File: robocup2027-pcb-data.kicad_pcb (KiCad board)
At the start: 6 copper layers, 83 x 117 mm, 47 parts, among them M5 Motor_Servo, M6 Motor_Servo, Q1 BPW40, Q2 BPW40, U1 ESP32-DEVKITC-32E

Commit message: updating pcb and step file
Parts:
- moved U12 31.5 mm to (151.9, 113.7)
- moved U4 27.9 mm to (120.6, 110.3)
- moved M6 12.8 mm to (128.3, 95.4)
- moved M5 10.3 mm to (149.7, 95.4)
- moved S1 0.78 mm to (121.4, 132.8)
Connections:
- U1 pad J2_12: unconnected-(U1-IO14-PadJ2_12) -> XSHUT1
- U1 pad J3_10: unconnected-(U1-IO5-PadJ3_10) -> XSHUT5
- U1 pad J3_16: unconnected-(U1-IO15-PadJ3_16) -> XSHUT6
- U1 pad J3_2: unconnected-(U1-IO23-PadJ3_2) -> XSHUT4
- U1 pad J3_8: unconnected-(U1-IO19-PadJ3_8) -> XSHUT3
- U1 pad J3_9: unconnected-(U1-IO18-PadJ3_9) -> XSHUT2
- U10 pad 5: unconnected-(U10-XSHUT-Pad5) -> XSHUT5
- U15 pad 5: unconnected-(U15-XSHUT-Pad5) -> XSHUT6
- U6 pad 5: unconnected-(U6-XSHUT-Pad5) -> XSHUT1
- U7 pad 5: unconnected-(U7-XSHUT-Pad5) -> XSHUT2
- U8 pad 5: unconnected-(U8-XSHUT-Pad5) -> XSHUT3
- U9 pad 5: unconnected-(U9-XSHUT-Pad5) -> XSHUT4

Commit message: some changes
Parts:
- moved U11 1.05 mm to (156.0, 56.8)
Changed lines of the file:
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@@
-		(embedded_fonts no)
-	)
-	(footprint "robo:DCDC-LTC3111"
-		(layer "F.Cu")
-		(at 155 56.5)
-		(property "Reference" "U11"
-			(at 0 -0.5 0)
-			(unlocked yes)
-			(layer "F.SilkS")
-			(effects
-				(font
-					(size 1 1)
-					(thickness 0.1)
-				)
-			)
-		)
-		(property "Value" "~"
-			(at 0 1 0)
-			(unlocked yes)
-			(layer "F.Fab")
-			(effects
-				(font
-					(size 1 1)
-					(thickness 0.15)
-				)
-			)
-		)
-		(property "Datasheet" ""
-			(at 0 0 0)
-			(unlocked yes)
-			(layer "F.Fab")
-			(hide yes)
-			(effects
-				(font
-					(size 1 1)
-					(thickness 0.15)
-				)
-			)
-		)
-		(property "Description" ""
-			(at 0 0 0)
-			(unlocked yes)
-			(layer "F.Fab")
-			(hide yes)
-			(effects
-				(font
-					(size 1 1)
-					(thickness 0.15)
-				)
-			)
-		)
-		(sheetname "/")
-		(sheetfile "robocup2027-pcb-data.kicad_sch")
-		(attr through_hole)
-		(fp_rect
-			(start -15 -15)
-			(end -15 15)
-			(stroke
-				(width 0.1)
-				(type default)
-			)
-			(fill no)
-			(layer "F.SilkS")
-		)
-		(fp_rect
-			(start -15 -15)
-			(end 15 -15)
-			(stroke
-				(width 0.1)
-				(type default)
-			)
-			(fill no)
-			(layer "F.SilkS")
-		)
-		(fp_rect
-			(start -15 15)
-			(end 15 15)
-			(stroke
-				(width 0.1)
-				(type default)
-			)
-			(fill no)
-			(layer "F.SilkS")
-		)
-		(fp_rect
-			(start 15 -15)
-			(end 15 15)
-			(stroke
-				(width 0.1)
-				(type default)
-			)
-			(fill no)
-			(layer "F.SilkS")
-		)
-		(fp_text user "Vout"
-			(at 6.1 -1.1 0)
-			(unlocked yes)
-			(layer "F.SilkS")
-			(effects
-				(font
-					(size 1 1)
-					(thickness 0.1)
-				)
-				(justify left bottom)
-			)
-		)
-		(fp_text user "Vin"
-			(at -9.2 -1.1 0)
-			(unlocked yes)
-			(layer "F.SilkS")
-			(effects
-				(font
-					(size 1 1)
-					(thickness 0.1)
-				)
-				(justify left bottom)
-			)
-		)
-		(fp_text user "GND"
-			(at 6.3 4.5 0)
-			(unlocked yes)
-			(layer "F.SilkS")
-			(effects
-				(font
-					(size 1 1)
-					(thickness 0.1)
-				)
-				(justify left bottom)
-			)
-		)
-		(fp_text user "GND"
-			(at -9.1 4.6 0)
-			(unlocked yes)
-			(layer "F.SilkS")
-			(effects
-				(font
-					(size 1 1)
-					(thickness 0.1)
-				)
-				(justify left bottom)
-			)
-		)
-		(fp_text user "${REFERENCE}"
-			(at 0 2.5 0)
-			(unlocked yes)
-			(layer "F.Fab")
-			(effects
-				(font
-					(size 1 1)
-					(thickness 0.15)
-				)
-			)
-		)
-		(pad "" thru_hole circle
-			(at -12 -12)
-			(size 2 2)
-			(drill 3.5)
-			(layers "*.Cu" "*.Mask")
-			(remove_unused_layers no)
-		)
-		(pad "" thru_hole circle
-			(at -12 12)
-			(size 2 2)
-			(drill 3.5)
-			(layers "*.Cu" "*.Mask")
-			(remove_unused_layers no)
-		)
-		(pad "" thru_hole circle
-			(at 0 12.5)
-			(size 2 2)
-			(drill 3.5)
-			(layers "*.Cu" "*.Mask")
-			(remove_unused_layers no)
-		)
-		(pad "" thru_hole circle
-			(at 12 -12)
-			(size 2 2)
-			(drill 3.5)
-			(layers "*.Cu" "*.Mask")
-			(remove_unused_layers no)
-		)
-		(pad "" thru_hole circle
-			(at 12 12)
-			(size 2 2)
-			(drill 3.5)
-			(layers "*.Cu" "*.Mask")
-			(remove_unused_layers no)
-		)
-		(pad "1" thru_hole circle
-			(at -11.8 -1.1)
-			(size 4 4)
-			(drill 2)
-			(layers "*.Cu" "*.Mask")
-			(remove_unused_layers no)
-			(net 14 "LiPo+")
-			(pinfunction "Vin")
-			(pintype "power_in")
-		)
-		(pad "2" thru_hole circle
-			(at -11.8 4)
-			(size 4 4)
-			(drill 2)
-			(layers "*.Cu" "*.Mask")
-			(remove_unused_layers no)
-			(net 2 "GND")
-			(pinfunction "GND")
-			(pintype "power_in")
-		)
-		(pad "3" thru_hole circle
-			(at 11.7 -1.1)
-			(size 4 4)
-			(drill 2)
-			(layers "*.Cu" "*.Mask")
-			(remove_unused_layers no)
-			(net 3 "+6V")
-			(pinfunction "Vout")
-			(pintype "power_in")
-		)
-		(pad "4" thru_hole circle
-			(at 11.7 4)
-			(size 4 4)
-			(drill 2)
-			(layers "*.Cu" "*.Mask")
-			(remove_unused_layers no)
-			(net 2 "GND")
-			(pinfunction "GND")
-			(pintype "power_in")
-		)
 		(embedded_fonts no)
 	)
@@
 		)
 		(embedded_fonts no)
+	)
+	(footprint "robo:DCDC-LTC3111"
+		(layer "F.Cu")
+		(at 156.01 56.79)
+		(property "Reference" "U11"
+			(at 0 -0.5 0)
+			(unlocked yes)
+			(layer "F.SilkS")
+			(effects
+				(font
+					(size 1 1)
+					(thickness 0.1)
+				)
+			)
+		)
+		(property "Value" "~"
+			(at 0 1 0)
+			(unlocked yes)
+			(layer "F.Fab")
+			(effects
+				(font
+					(size 1 1)
+					(thickness 0.15)
+				)
+			)
+		)
+		(property "Datasheet" ""
+			(at 0 0 0)
+			(unlocked yes)
+			(layer "F.Fab")
+			(hide yes)
+			(effects
+				(font
+					(size 1 1)
+					(thickness 0.15)
+				)
+			)
+		)
+		(property "Description" ""
+			(at 0 0 0)
+			(unlocked yes)
+			(layer "F.Fab")
+			(hide yes)
+			(effects
+				(font
+					(size 1 1)
+					(thickness 0.15)
+				)
+			)
+		)
+		(sheetname "/")
+		(sheetfile "robocup2027-pcb-data.kicad_sch")
+		(attr through_hole)
+		(fp_rect
+			(start -15 -15)
+			(end -15 15)
+			(stroke
+				(width 0.1)
+				(type default)
+			)
+			(fill no)
+			(layer "F.SilkS")
+		)
+		(fp_rect
+			(start -15 -15)
+			(end 15 -15)
+			(stroke
+				(width 0.1)
+				(type default)
+			)
+			(fill no)
+			(layer "F.SilkS")
+		)
+		(fp_rect
+			(start -15 15)
+			(end 15 15)
+			(stroke
+				(width 0.1)
+				(type default)
+			)
+			(fill no)
+			(layer "F.SilkS")
+		)
+		(fp_rect
+			(start 15 -15)
+			(end 15 15)
+			(stroke
+				(width 0.1)
+				(type default)
+			)
+			(fill no)
+			(layer "F.SilkS")
+		)
+		(fp_text user "GND"
+			(at -9.1 4.6 0)
+			(unlocked yes)
+			(layer "F.SilkS")
+			(effects
+				(font
+					(size 1 1)
+					(thickness 0.1)
+				)
+				(justify left bottom)
+			)
+		)
+		(fp_text user "Vin"
+			(at -9.2 -1.1 0)
+			(unlocked yes)
+			(layer "F.SilkS")
+			(effects
+				(font
+					(size 1 1)
+					(thickness 0.1)
+				)
+				(justify left bottom)
+			)
+		)
+		(fp_text user "Vout"
+			(at 6.1 -1.1 0)
+			(unlocked yes)
+			(layer "F.SilkS")
+			(effects
+				(font
+					(size 1 1)
+					(thickness 0.1)
+				)
+				(justify left bottom)
+			)
+		)
+		(fp_text user "GND"
+			(at 6.3 4.5 0)
+			(unlocked yes)
+			(layer "F.SilkS")
+			(effects
+				(font
+					(size 1 1)
+					(thickness 0.1)
+				)
+				(justify left bottom)
+			)
+		)
+		(fp_text user "${REFERENCE}"
+			(at 0 2.5 0)
+			(unlocked yes)
+			(layer "F.Fab")
+			(effects
+				(font
+					(size 1 1)
+					(thickness 0.15)
+				)
+			)
+		)
+		(pad "" thru_hole circle
+			(at -12 -12)
+			(size 2 2)
+			(drill 3.5)
+			(layers "*.Mask")
+			(remove_unused_layers no)
+		)
+		(pad "" thru_hole circle
+			(at -12 12)
+			(size 2 2)
+			(drill 3.5)
+			(layers "*.Mask")
+			(remove_unused_layers no)
+		)
+		(pad "" thru_hole rect
+			(at -10.9 -6.5)
+			(size 2 2)
+			(drill oval 7 3.5)
+			(layers "*.Mask")
+			(remove_unused_layers no)
+		)
+		(pad "" thru_hole rect
+			(at 0 -12)
+			(size 2 2)
+			(drill oval 7.5 3.5)
+			(layers "*.Mask")
+			(remove_unused_layers no)
+		)
+		(pad "" thru_hole circle
+			(at 0 12.5)
+			(size 2 2)
+			(drill 3.5)
+			(layers "*.Mask")
+			(remove_unused_layers no)
+		)
+		(pad "" thru_hole circle
+			(at 12 -12)
+			(size 2 2)
+			(drill 3.5)
+			(layers "*.Mask")
+			(remove_unused_layers no)
+		)
+		(pad "" thru_hole circle
+			(at 12 12)
+			(size 2 2)
+			(drill 3.5)
+			(layers "*.Mask")
+			(remove_unused_layers no)
+		)
+		(pad "1" thru_hole circle
+			(at -11.8 -1.1)
+			(size 4 4)
+			(drill 2)
+			(layers "*.Cu" "*.Mask")
+			(remove_unused_layers no)
+			(net 14 "LiPo+")
+			(pinfunction "Vin")
+			(pintype "power_in")
+		)
+		(pad "2" thru_hole circle
+			(at -11.8 4)
+			(size 4 4)
+			(drill 2)
+			(layers "*.Cu" "*.Mask")
+			(remove_unused_layers no)
+			(net 2 "GND")
+			(pinfunction "GND")
+			(pintype "power_in")
+		)
+		(pad "3" thru_hole circle
+			(at 11.7 -1.1)
+			(size 4 4)
+			(drill 2)
+			(layers "*.Cu" "*.Mask")
+			(remove_unused_layers no)
+			(net 3 "+6V")
+			(pinfunction "Vout")
+			(pintype "power_in")
+		)
+		(pad "4" thru_hole circle
+			(at 11.7 4)
+			(size 4 4)
+			(drill 2)
+			(layers "*.Cu" "*.Mask")
+			(remove_unused_layers no)
+			(net 2 "GND")
+			(pinfunction "GND")
+			(pintype "power_in")
+		)
+		(embedded_fonts no)

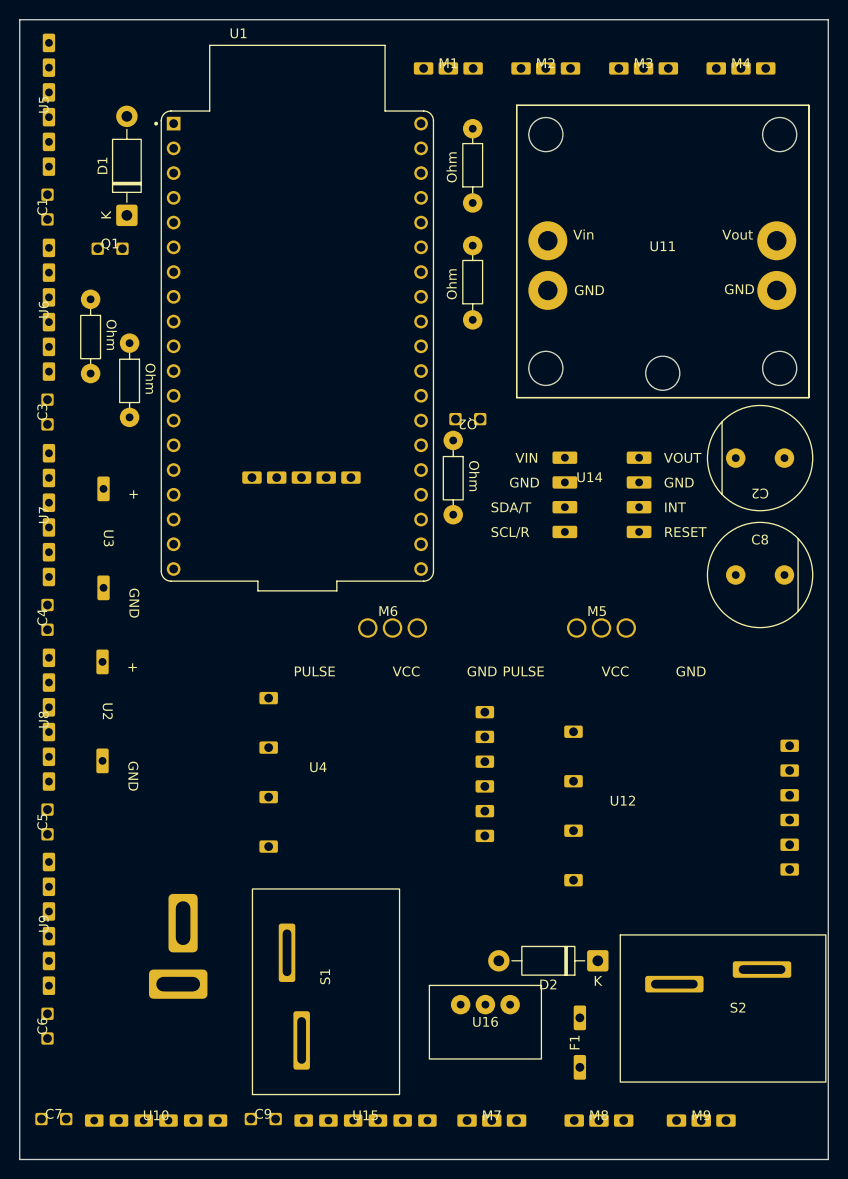
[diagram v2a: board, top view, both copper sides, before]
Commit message: fix: add vias and replace gyro
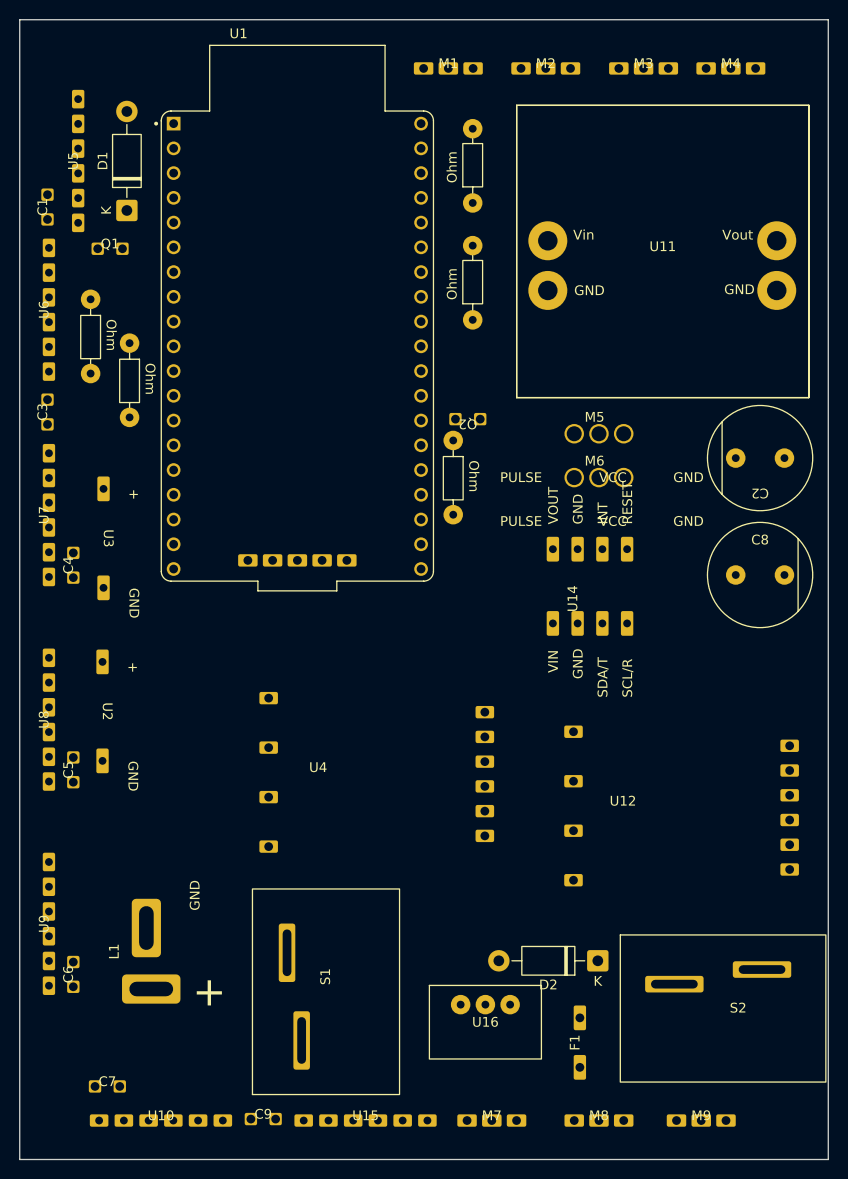
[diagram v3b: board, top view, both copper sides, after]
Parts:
- added ?: , , F.Cu at (169.5, 36.5)
- added ?: , , F.Cu at (93.5, 146.5)
- added ?: , , F.Cu at (93.5, 36.5)
- added ?: , , F.Cu at (169.5, 146.5)
- L1: moved to F.Cu
- moved M6 26.2 mm to (149.5, 80.0)
- moved M5 19.9 mm to (149.5, 75.5)
- moved U14 12.0 mm to (147.3, 92.4), turned to 90 degrees
- moved U13 8.51 mm to (118.5, 88.5)
- moved U5 6.50 mm to (96.0, 47.5)
- moved C7 6.44 mm to (99.0, 142.5)
- moved C4 5.97 mm to (95.5, 89.0)
- moved C5 5.97 mm to (95.5, 110.0)
- moved C6 5.93 mm to (95.5, 131.0)
- moved L1 2.81 mm to (103.5, 127.0)
- moved M4 1.04 mm to (163.0, 38.0)
- moved D1 0.50 mm to (101.0, 52.6)
- moved U10 0.50 mm to (104.5, 146.0)

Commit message: edit print
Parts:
- moved C9 5.54 mm to (120.5, 145.6)
- moved Q2 2.80 mm to (136.0, 71.2)
- moved C3 1.87 mm to (94.6, 72.6)
- moved U15 1.63 mm to (125.8, 147.6)
- moved C7 0.64 mm to (99.4, 143.0)
- renumbered U14 to Gyro
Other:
- board text added: "1000uF"
- board text added: "470uF"
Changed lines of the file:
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@@
 		(at 149.46 146)
 		(property "Reference" "M8"
-			(at 0 -0.5 0)
+			(at -0.06 -1.8 0)
 			(unlocked yes)
 			(layer "F.SilkS")
@@
 		(at 95.5 89 90)
 		(property "Reference" "C4"
-			(at 0 -0.5 90)
+			(at 3.6 -0.3 90)
 			(unlocked yes)
 			(layer "F.SilkS")
@@
 		(at 92.85 52.23 90)
 		(property "Reference" "C1"
-			(at 0 -0.5 90)
+			(at 3.63 -0.05 90)
 			(unlocked yes)
 			(layer "F.SilkS")
@@
 	(footprint "robo:2.54mm_capacitor"
 		(layer "F.Cu")
-		(at 115 145.85)
+		(at 120.53 145.6)
 		(property "Reference" "C9"
-			(at 0 -0.5 0)
+			(at 3.47 0 0)
 			(unlocked yes)
 			(layer "F.SilkS")
@@
 			(layer "F.SilkS")
 		)
-		(fp_text user "Ohm"
+		(fp_text user "SDA"
 			(at -1.778 -1.524 90)
 			(unlocked yes)
@@
 		(at 134 38)
 		(property "Reference" "M1"
-			(at 0 -0.5 0)
+			(at -0.02 -1.6 0)
 			(unlocked yes)
 			(layer "F.SilkS")
@@
 		(at 149.46 75.5)
 		(property "Reference" "M5"
-			(at -0.45 -1.7 0)
+			(at -4.86 -0.1 0)
 			(unlocked yes)
 			(layer "F.SilkS")
@@
 		)
 		(fp_text user "VCC"
-			(at 0 5.08 0)
+			(at -1.46 -1.3 0)
 			(unlocked yes)
 			(layer "F.SilkS")
@@
 		)
 		(fp_text user "PULSE"
-			(at -10.16 5.08 0)
+			(at -7.26 -1.3 0)
 			(unlocked yes)
 			(layer "F.SilkS")
@@
 		)
 		(fp_text user "GND"
-			(at 7.62 5.08 0)
+			(at 1.74 -1.5 0)
 			(unlocked yes)
 			(layer "F.SilkS")
@@
 	(footprint "robo:VL53L1X-ToF"
 		(layer "F.Cu")
-		(at 125.5 146)
+		(at 125.8 147.6)
 		(property "Reference" "U15"
-			(at 0 -0.5 0)
+			(at 1.6 -2 0)
 			(unlocked yes)
 			(layer "F.SilkS")
@@
 		(at 96 47.5 90)
 		(property "Reference" "U5"
-			(at 0 -0.5 90)
+			(at 0 -1.4 90)
 			(unlocked yes)
 			(layer "F.SilkS")
@@
 	(footprint "robo:2.54mm_capacitor"
 		(layer "F.Cu")
-		(at 136 74 180)
+		(at 136 71.2 180)
 		(property "Reference" "Q2"
-			(at 0 -0.5 180)
+			(at 0 -1.6 180)
 			(unlocked yes)
 			(layer "F.SilkS")
@@
 		(at 138.46 146)
 		(property "Reference" "M7"
-			(at 0 -0.5 0)
+			(at -0.06 -1.8 0)
 			(unlocked yes)
 			(layer "F.SilkS")
@@
 		(at 93 83.85 90)
 		(property "Reference" "U7"
-			(at 0 -0.5 90)
+			(at 0.25 -1.6 90)
 			(unlocked yes)
 			(layer "F.SilkS")
@@
 		(at 93 104.85 90)
 		(property "Reference" "U8"
-			(at 0 -0.5 90)
+			(at 0 -1.6 90)
 			(unlocked yes)
 			(layer "F.SilkS")
@@
 		(at 163 38)
 		(property "Reference" "M4"
-			(at 0 -0.5 0)
+			(at 0 -1.6 0)
 			(unlocked yes)
 			(layer "F.SilkS")
@@
 		(at 159.96 146)
 		(property "Reference" "M9"
-			(at 0 -0.5 0)
+			(at 0 -1.6 0)
 			(unlocked yes)
 			(layer "F.SilkS")
@@
 		(at 95.5 110 90)
 		(property "Reference" "C5"
-			(at 0 -0.5 90)
+			(at 3.2 -0.1 90)
 			(unlocked yes)
 			(layer "F.SilkS")
@@
 	(footprint "robo:2.54mm_capacitor"
 		(layer "F.Cu")
-		(at 99 142.5)
+		(at 99.4 143)
 		(property "Reference" "C7"
-			(at 0 -0.5 0)
+			(at 3.4 0 0)
 			(unlocked yes)
 			(layer "F.SilkS")
@@
 			(layer "F.SilkS")
 		)
-		(fp_text user "Ohm"
+		(fp_text user "100k"
 			(at -1.778 -1.524 270)
 			(unlocked yes)
@@
 		(at 93 125.81 90)
 		(property "Reference" "U9"
-			(at 0 -0.5 90)
+			(at 0.01 -1.6 90)
 			(unlocked yes)
 			(layer "F.SilkS")
@@
 			(layer "F.CrtYd")
 		)
-		(fp_text user "GND"
-			(at 7.62 5.08 0)
-			(unlocked yes)
-			(layer "F.SilkS")
-			(effects
-				(font
-					(size 1 1)
-					(thickness 0.1)
-				)
-				(justify left bottom)
-			)
-		)
-		(fp_text user "PULSE"
-			(at -10.16 5.08 0)
-			(unlocked yes)
-			(layer "F.SilkS")
-			(effects
-				(font
-					(size 1 1)
-					(thickness 0.1)
-				)
-				(justify left bottom)
-			)
-		)
 		(fp_text user "VCC"
-			(at 0 5.08 0)
+			(at 4.34 3.6 0)
 			(unlocked yes)
 			(layer "F.SilkS")
@@
 	(footprint "robo:2.54mm_capacitor"
 		(layer "F.Cu")
-		(at 92.85 73.27 90)
+		(at 94.6 72.6 90)
 		(property "Reference" "C3"
-			(at 0 -0.5 90)
+			(at 0 -1.6 90)
 			(unlocked yes)
 			(layer "F.SilkS")
@@
 		(at 144 38)
 		(property "Reference" "M2"
-			(at 0 -0.5 0)
+			(at -0.01 -1.6 0)
 			(unlocked yes)
 			(layer "F.SilkS")
@@
 			(layer "F.SilkS")
 		)
-		(fp_text user "Ohm"
+		(fp_text user "100k"
 			(at -1.778 -1.524 270)
 			(unlocked yes)
@@
 		(at 166 78 180)
 		(property "Reference" "C2"
-			(at 0 -3.6 180)
+			(at 0 -3.6 0)
 			(unlocked yes)
 			(layer "F.SilkS")
@@
 		(at 154.04 38)
 		(property "Reference" "M3"
-			(at 0 -0.5 0)
+			(at -0.1 -1.6 0)
 			(unlocked yes)
 			(layer "F.SilkS")
@@
 		(tags "Diode DO-41_SOD81 series Axial Horizontal pin pitch 10.16mm  length 5.2mm diameter 2.7mm")
 		(property "Reference" "D2"
-			(at 5.08 -2.47 0)
+			(at 4.142 -2.597 0)
 			(layer "F.SilkS")
 			(effects
@@
 		(at 99.277 56.51)
 		(property "Reference" "Q1"
-			(at 0 -0.5 0)
+			(at -0.077 -1.51 0)
 			(unlocked yes)
 			(layer "F.SilkS")
@@
 		(at 95.5 131 90)
 		(property "Reference" "C6"
-			(at 0 -0.5 90)
+			(at 3.4 0.1 90)
 			(unlocked yes)
 			(layer "F.SilkS")
@@
 		(at 93 62.77 90)
 		(property "Reference" "U6"
-			(at 0 -0.5 90)
+			(at 0.17 1.8 90)
 			(unlocked yes)
 			(layer "F.SilkS")
@@
 		(layer "F.Cu")
 		(at 147.27 92.43 90)
-		(property "Reference" "U14"
-			(at 0 -0.5 90)
+		(property "Reference" "Gyro"
+			(at 1.03 -0.5 0)
 			(unlocked yes)
 			(layer "F.SilkS")
@@
 			(layer "F.SilkS")
 		)
-		(fp_text user "Ohm"
+		(fp_text user "100k"
 			(at -1.778 -1.524 270)
 			(unlocked yes)
@@
 		(at 104.5 146)
 		(property "Reference" "U10"
-			(at 0 -0.5 0)
+			(at 0 -1.6 0)
 			(unlocked yes)
 			(layer "F.SilkS")
@@
 			(layer "F.SilkS")
 		)
-		(fp_text user "Ohm"
+		(fp_text user "SCL"
 			(at -1.778 -1.524 90)
 			(unlocked yes)
@@
 		(layer "Edge.Cuts")
 	)
+	(gr_text "470uF"
+		(at 162.4 93.6 0)
+		(layer "F.SilkS")
+		(effects
+			(font
+				(size 1.5 1.5)
+				(thickness 0.1875)
+			)
+			(justify left bottom)
+		)
+	)
+	(gr_text "1000uF"
+		(at 162.8 75.8 0)
+		(layer "F.SilkS")
+		(effects
+			(font
+				(size 1.5 1.5)
+				(thickness 0.1875)
+			)
+			(justify left bottom)
+		)
+	)
 	(embedded_fonts no)
